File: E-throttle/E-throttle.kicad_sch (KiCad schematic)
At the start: 48 parts, among them IC1 BTS441TG, J1 Micro_SD_Card_Det1, J3 Conn_01x11, J4 Conn_01x11, J5 776087-1, Q1 NMOS, SW1 SW_Push, U1 74HC123, U2 LM317_SOT-223, U3 LM317_SOT-223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

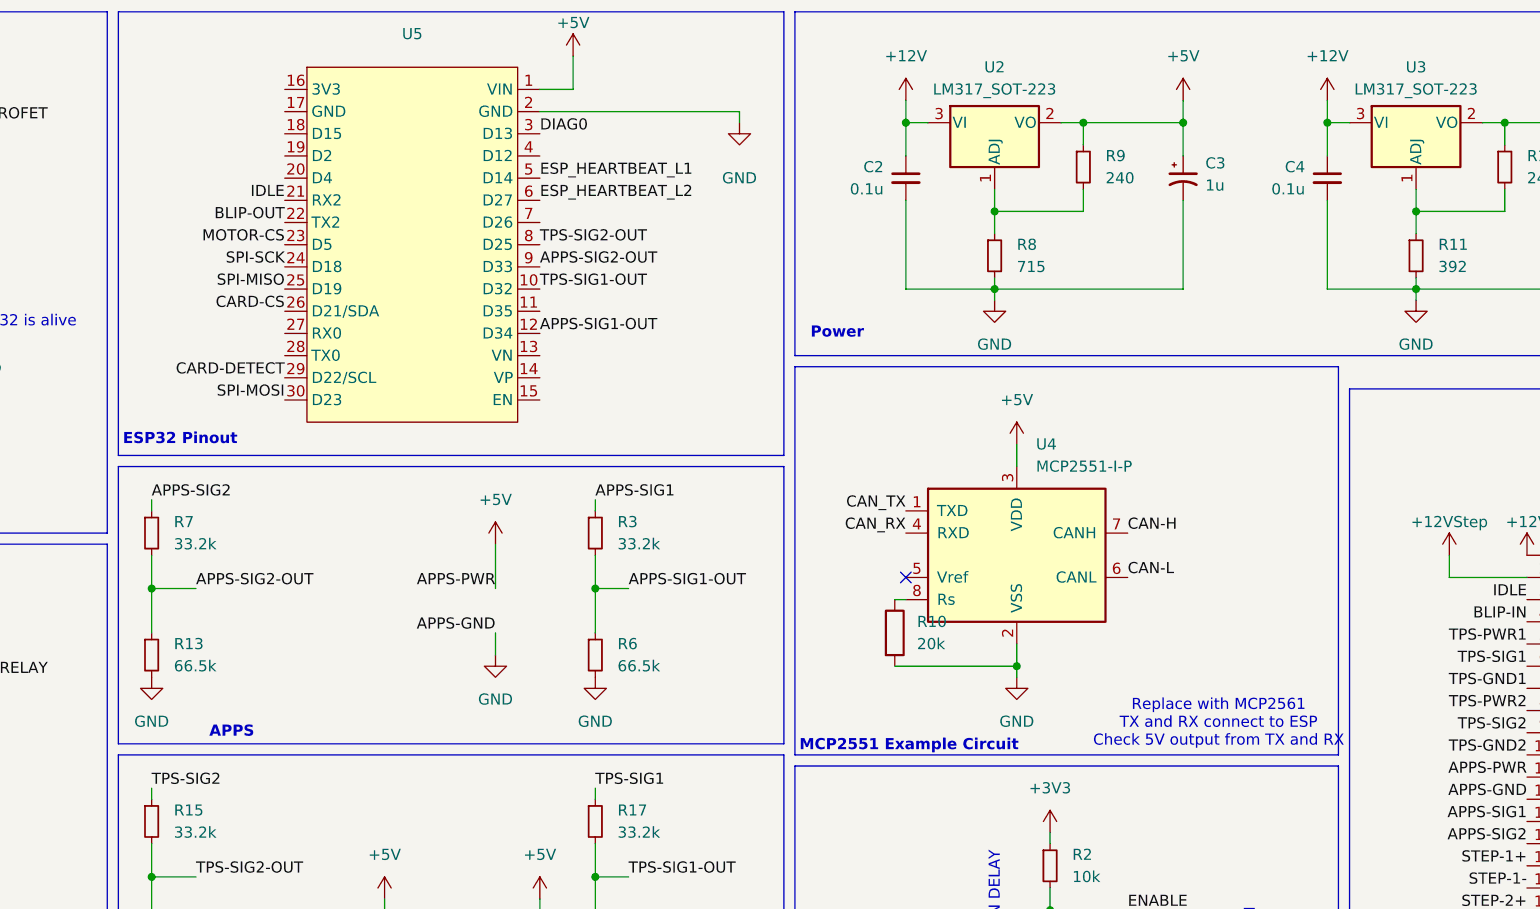
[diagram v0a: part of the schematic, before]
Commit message: Adjusted layout, added ground plane
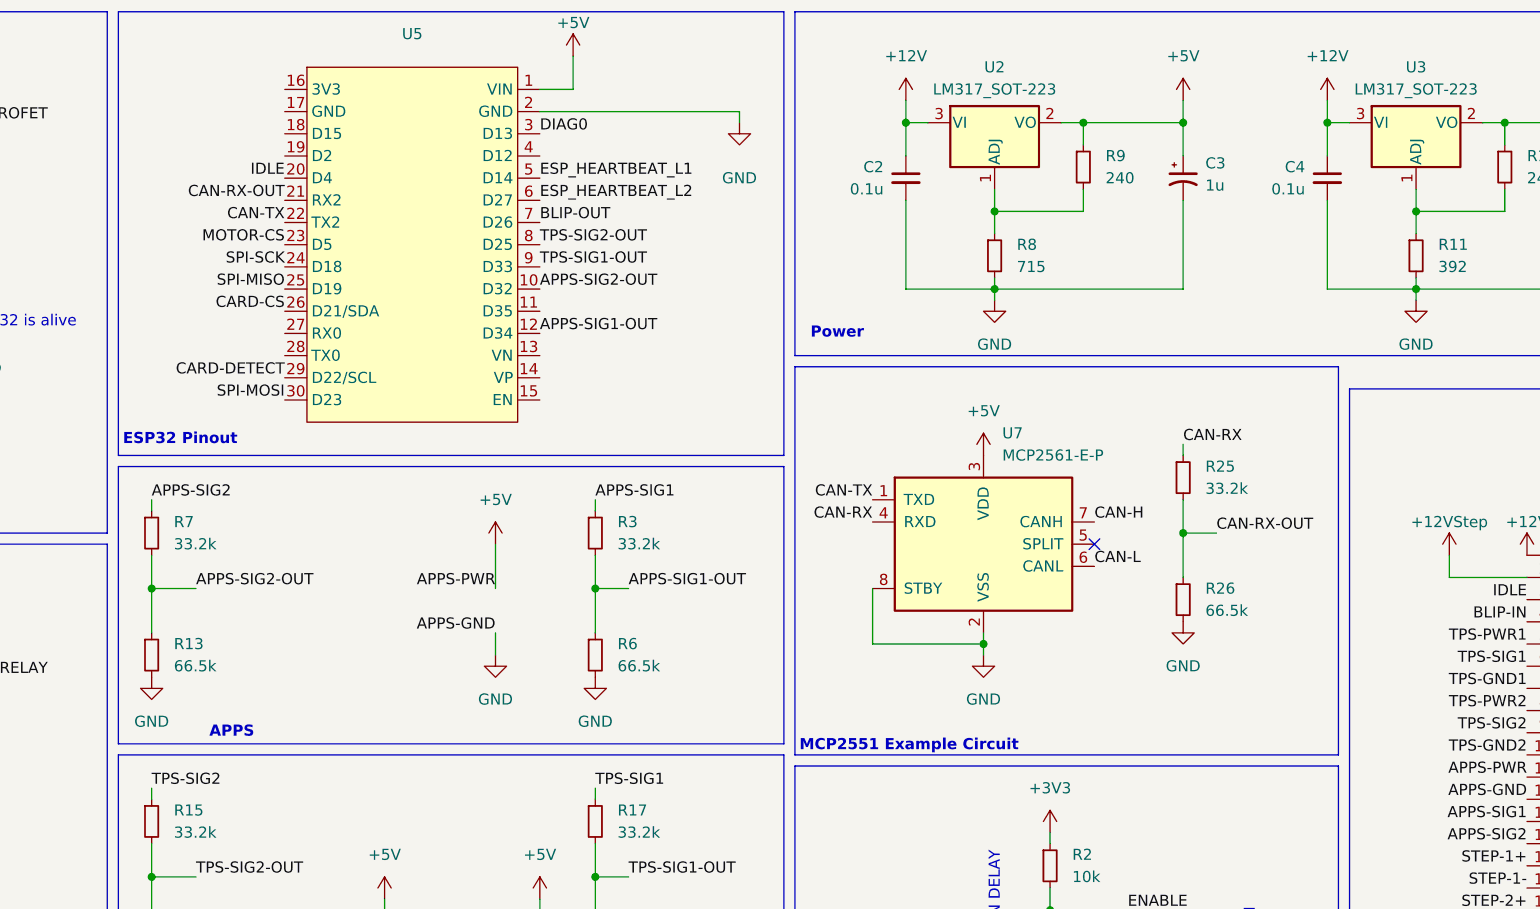
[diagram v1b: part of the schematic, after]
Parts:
- removed R10: 20k, Resistor_THT:R_Axial_DIN0207_L6.3mm_D2.5mm_P10.16mm_Horizontal, symbol Device:R
- removed U4: MCP2551-I-P, Package_DIP:DIP-8_W7.62mm, symbol Interface_CAN_LIN:MCP2551-I-P
- added R25: 33.2k, Resistor_THT:R_Axial_DIN0207_L6.3mm_D2.5mm_P10.16mm_Horizontal, symbol Device:R_Small
- added R26: 66.5k, Resistor_THT:R_Axial_DIN0207_L6.3mm_D2.5mm_P10.16mm_Horizontal, symbol Device:R_Small
- added U7: MCP2561-E-P, Package_DIP:DIP-8_W7.62mm, symbol Interface_CAN_LIN:MCP2561-E-P
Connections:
- net +5V: now also U7.3 (VDD)
- net APPS-SIG2-OUT: now also U5.10 (D32); no longer U5.9 (D33)
- net BLIP-OUT: now also U5.7 (D26); no longer U5.22 (TX2)
- net CAN-H: now also U7.7 (CANH)
- net CAN-L: now also U7.6 (CANL)
- net GND: now also R26.2, U7.2 (VSS), U7.8 (STBY)
- net IDLE: now also U5.20 (D4); no longer U5.21 (RX2)
- net TPS-SIG1-OUT: now also U5.9 (D33); no longer U5.10 (D32)
- new net CAN-RX: R25.1, U7.4 (RXD)
- new net CAN-RX-OUT: R25.2, R26.1, U5.21 (RX2)
- new net CAN-TX: U5.22 (TX2), U7.1 (TXD)
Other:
- note removed: "Replace with MCP2561 TX and RX connect to ESP Check 5V output from TX and RX"

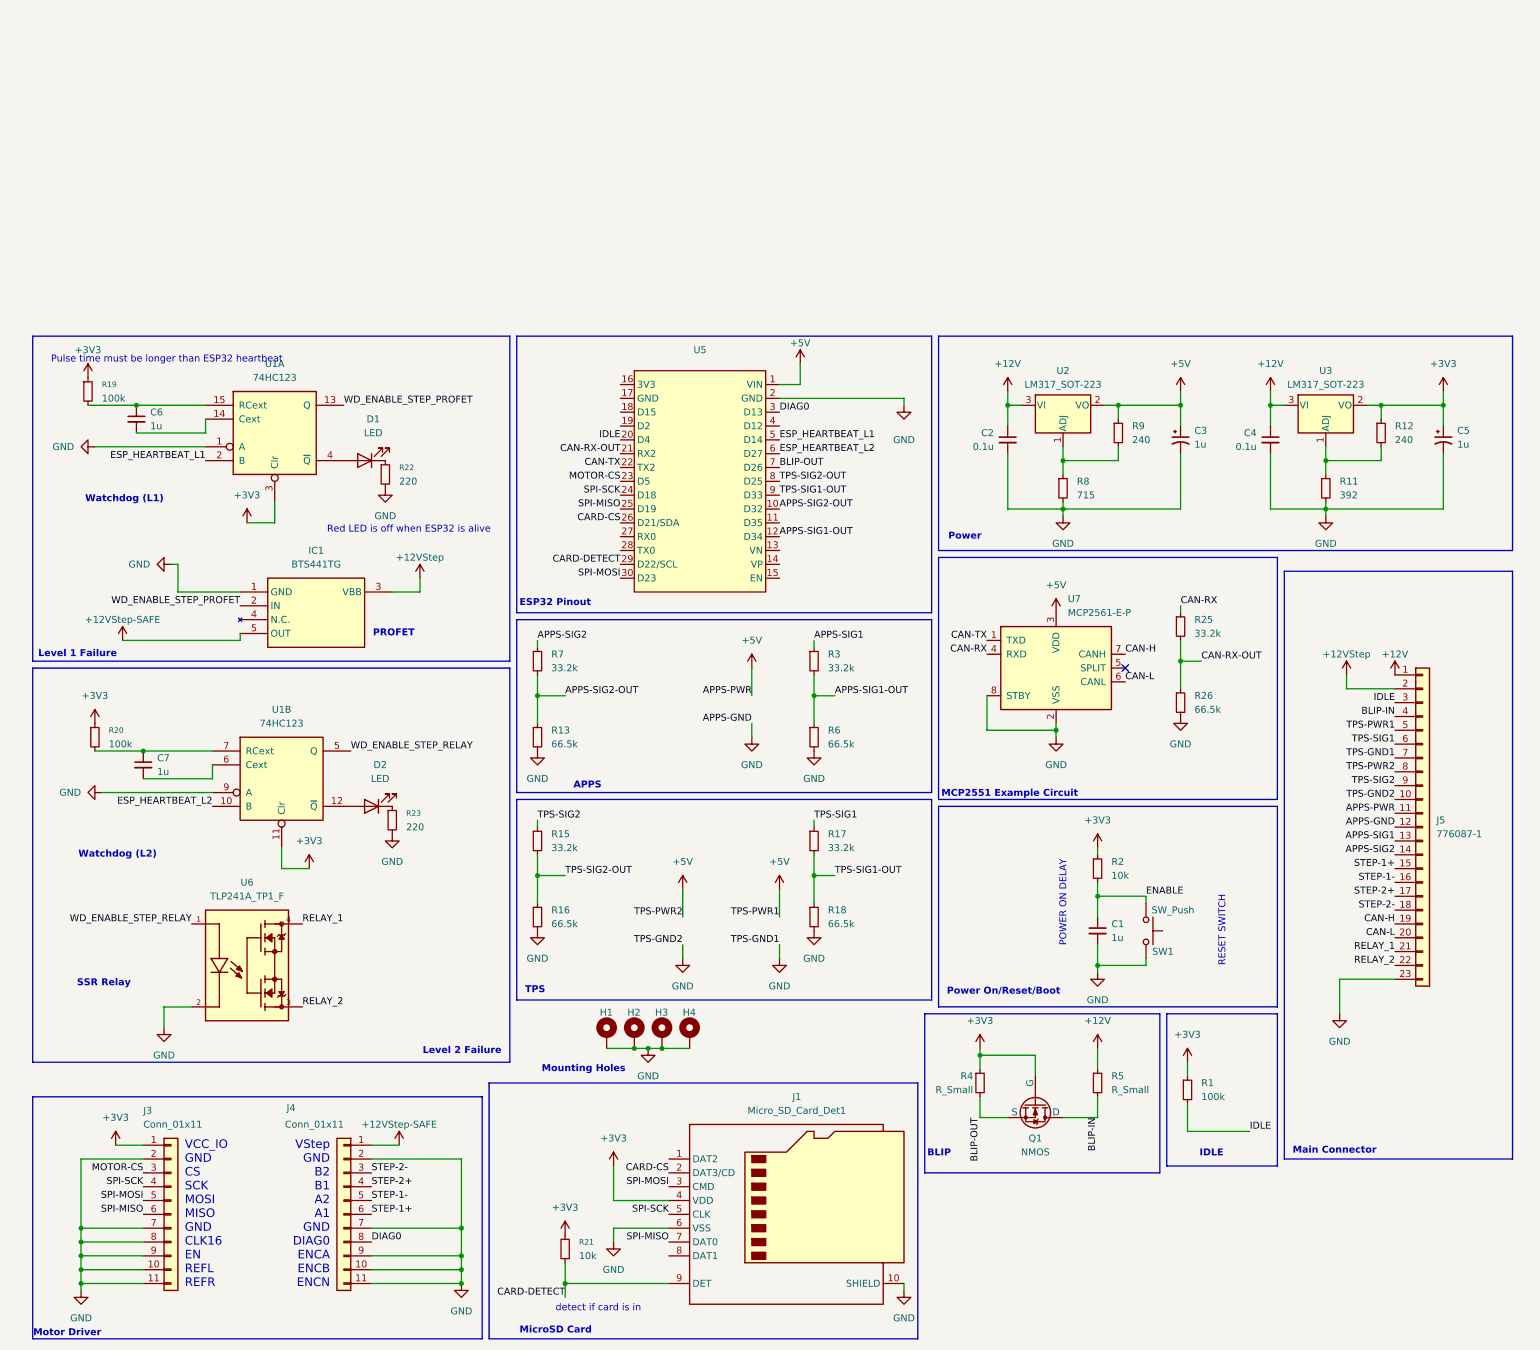
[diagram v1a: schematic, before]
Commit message: Finalized Schematic (added power status LEDs, pull-up resistors for SD, separate 5V power) - not reviewed yet
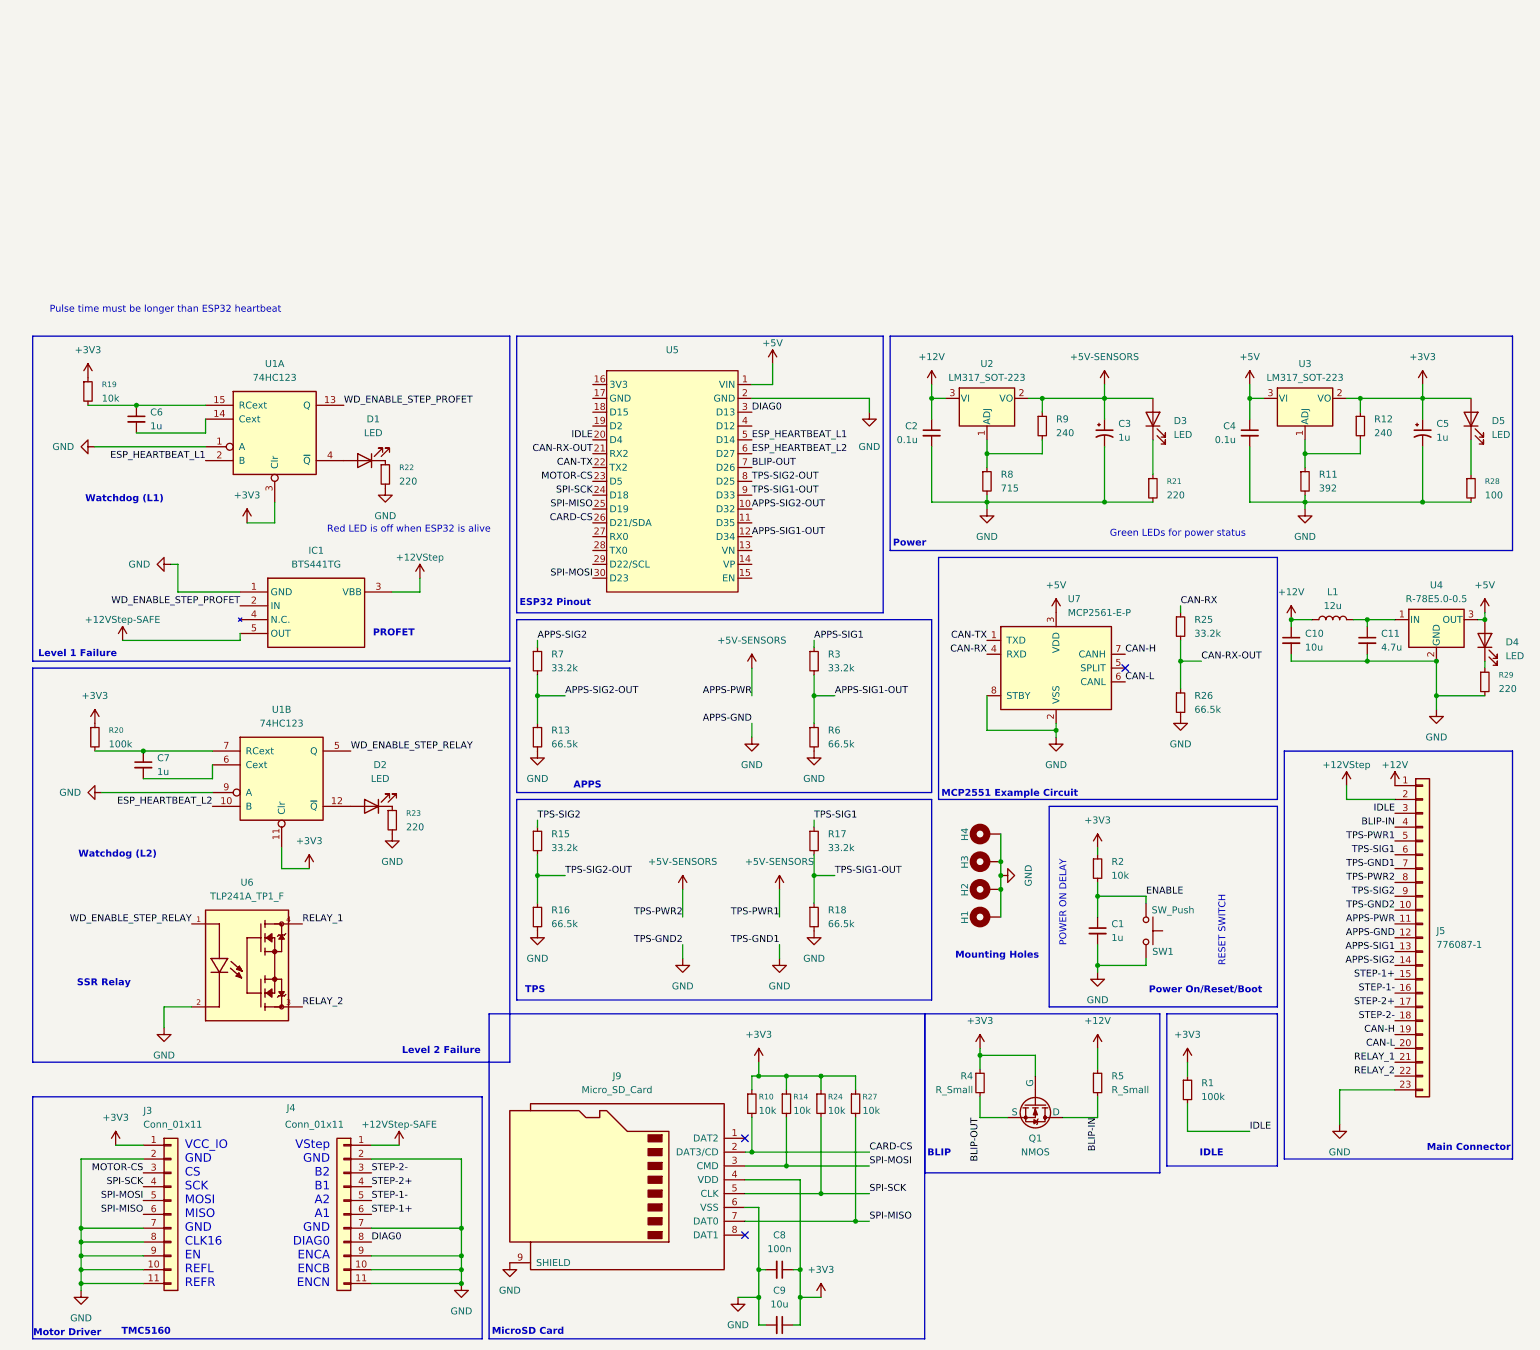
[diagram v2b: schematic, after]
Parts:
- removed J1: Micro_SD_Card_Det1, Connector_Card:microSD_HC_Hirose_DM3AT-SF-PEJM5, symbol Connector:Micro_SD_Card_Det1
- added C10: 10u, Capacitor_SMD:C_0603_1608Metric_Pad1.08x0.95mm_HandSolder, symbol Device:C_Small
- added C11: 4.7u, Capacitor_SMD:C_0603_1608Metric_Pad1.08x0.95mm_HandSolder, symbol Device:C_Small
- added C8: 100n, Capacitor_SMD:C_0805_2012Metric, symbol Device:C_Small
- added C9: 10u, Capacitor_SMD:C_0805_2012Metric, symbol Device:C_Small
- added D3, D4, D5: LED, symbol Device:LED
- added J9: Micro_SD_Card, Connector_Card:microSD_HC_Wuerth_693072010801, symbol Connector:Micro_SD_Card
- added L1: 12u, Inductor_SMD:L_6.3x6.3_H3, symbol Device:L
- added R10, R14, R24, R27: 10k, Resistor_SMD:R_0805_2012Metric, symbol Device:R_Small
- added R28: 100, symbol Device:R_Small
- added R29: 220, symbol Device:R_Small
- added U4: R-78E5.0-0.5, Converter_DCDC:Converter_DCDC_RECOM_R-78E-0.5_THT, symbol Regulator_Switching:R-78E5.0-0.5
- C1, C2, C3, C4, C5, C6, C7: footprint Capacitor_THT:C_Disc_D5.0mm_W2.5mm_P2.50mm -> Capacitor_SMD:C_0805_2012Metric
- R1, R11, R12, R13, R15, R16, R17, R18, R2, R20, R22, R23, R25, R26, R3, R4, R5, R6, R7, R8, R9: footprint Resistor_THT:R_Axial_DIN0207_L6.3mm_D2.5mm_P10.16mm_Horizontal -> Resistor_SMD:R_0805_2012Metric
- R19: value 100k -> 10k; footprint Resistor_THT:R_Axial_DIN0207_L6.3mm_D2.5mm_P10.16mm_Horizontal -> Resistor_SMD:R_0805_2012Metric
- R21: value 10k -> 220; footprint Resistor_THT:R_Axial_DIN0207_L6.3mm_D2.5mm_P10.16mm_Horizontal -> (none)
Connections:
- net +12V: now also C10.1, L1.1; no longer C4.1, U3.3 (VI)
- net +3V3: now also C8.1, C9.1, D5.2 (A), J9.4 (VDD), R10.1, R14.1, R24.1, R27.1; no longer R21.2
- net +5V: now also C4.1, U3.3 (VI), D4.2 (A), U4.3 (OUT); no longer C3.1, J5.11 (Pin_11), J5.5 (Pin_5), J5.8 (Pin_8), R9.1, U2.2 (VO)
- net CARD-CS: now also J9.2 (DAT3/CD), R10.2
- net GND: now also R21.2, C10.2, C11.2, C8.2, C9.2, J9.6 (VSS), J9.9 (SHIELD), R28.2, R29.2, U4.2 (GND)
- net SPI-MISO: now also J9.7 (DAT0), R27.2
- net SPI-MOSI: now also J9.3 (CMD), R14.2
- net SPI-SCK: now also J9.5 (CLK), R24.2
- net CARD-DETECT: no longer names the net of R21.1
- net CARD-DETECT: now also D3.1 (K); no longer U5.29 (D22/SCL)
- new net: D5.1 (K), R28.1
- new net: D4.1 (K), R29.1
- new net: C11.1, L1.2, U4.1 (IN)
- new net +5V-SENSORS: C3.1, D3.2 (A), J5.11 (Pin_11), J5.5 (Pin_5), J5.8 (Pin_8), R9.1, U2.2 (VO)
- no-connect marks 1 -> 3
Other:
- note added: "Green LEDs for power status"
- note added: "TMC5160"
- note removed: "detect if card is in"
- moved on the sheet: C2, C3, C4, C5, H1, H2, H3, H4, J5, R11, R12, R8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

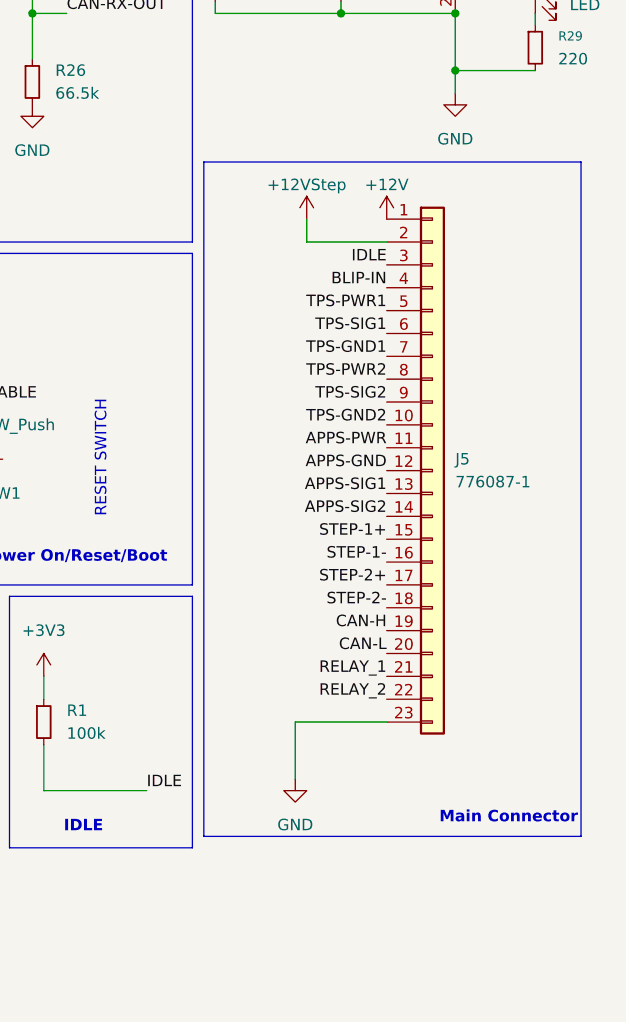
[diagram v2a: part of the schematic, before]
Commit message: (Actually) finalized schematic - added status LED for 12V supply - need to review
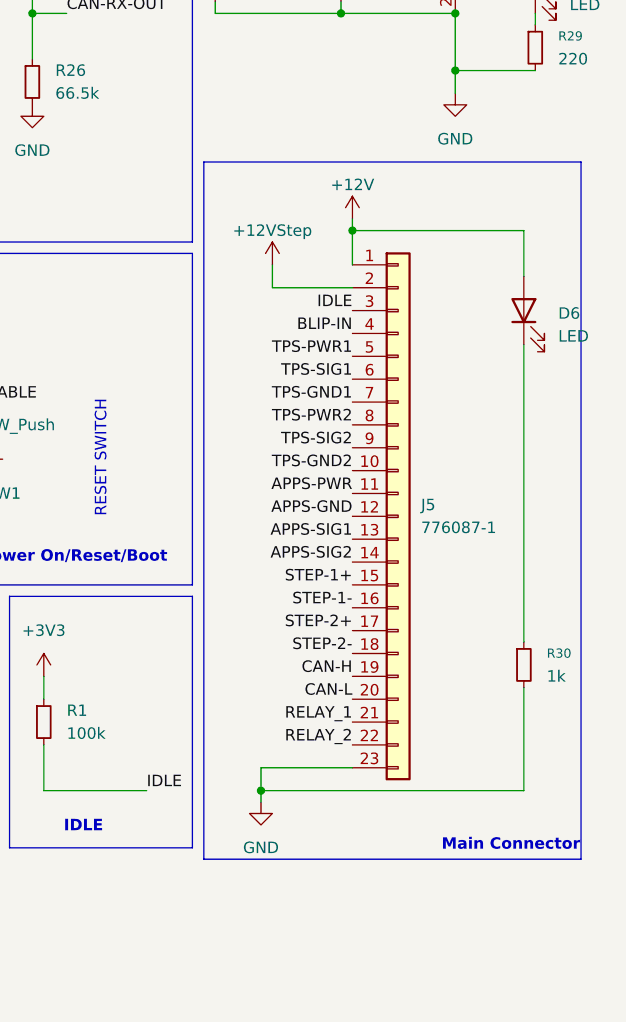
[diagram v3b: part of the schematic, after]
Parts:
- added D6: LED, symbol Device:LED
- added R30: 1k, symbol Device:R_Small
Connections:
- net +12V: now also D6.2 (A)
- net GND: now also R30.2
- new net: D6.1 (K), R30.1
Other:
- moved on the sheet: J5
